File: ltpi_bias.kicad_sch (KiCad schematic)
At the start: 18 parts

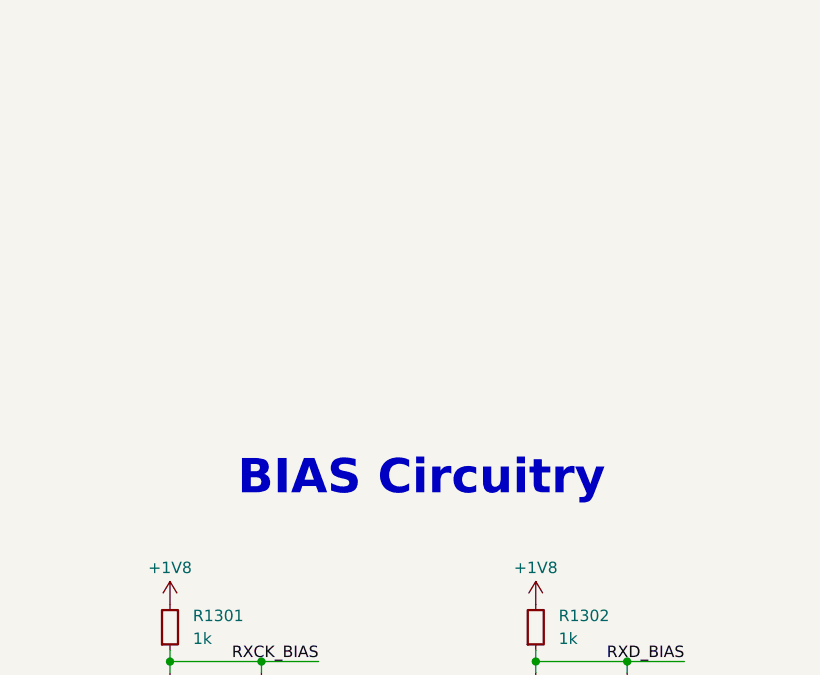
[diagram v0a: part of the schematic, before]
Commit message: [#100282] Add missing schematic sheet names and align them all
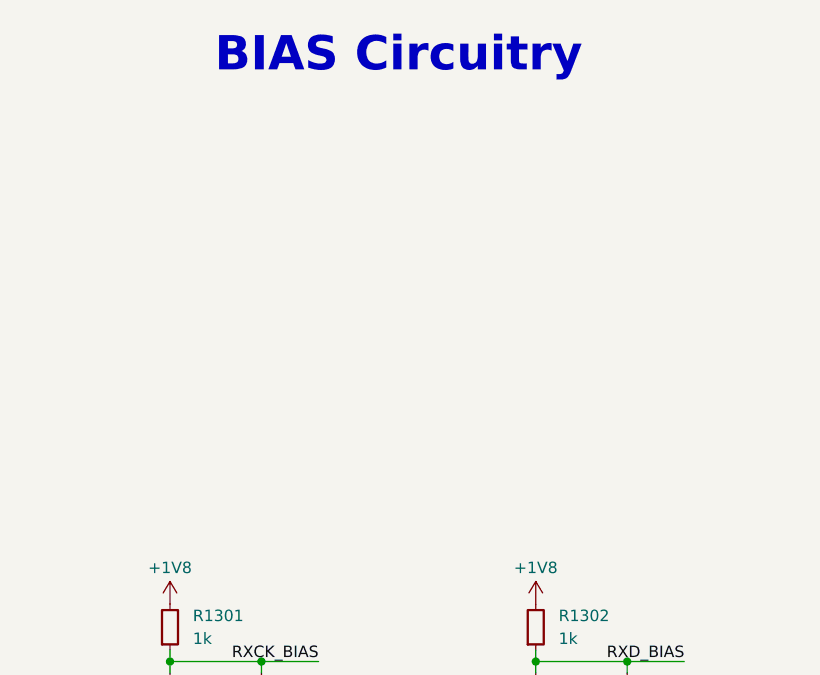
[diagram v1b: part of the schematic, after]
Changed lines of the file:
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@@
 	(text "BIAS Circuitry"
 		(exclude_from_sim no)
-		(at 213.36 85.09 0)
+		(at 210.82 38.1 0)
 		(effects
 			(font

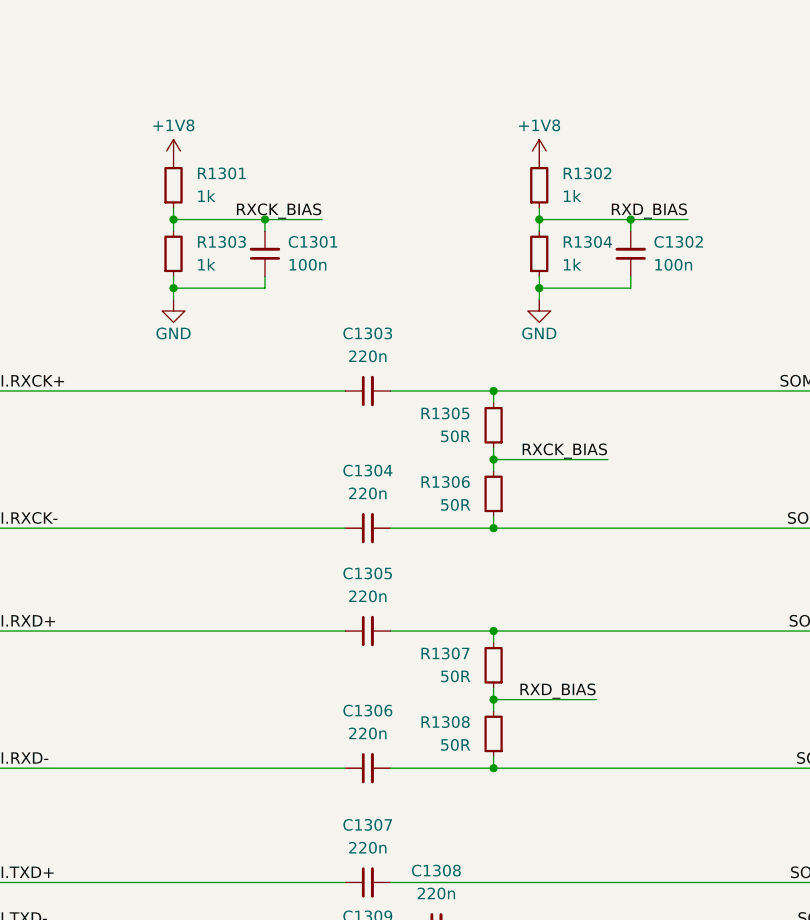
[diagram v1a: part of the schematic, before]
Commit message: [#100501] Replace 50R resistors with 49R9 in LTPI bias circuit
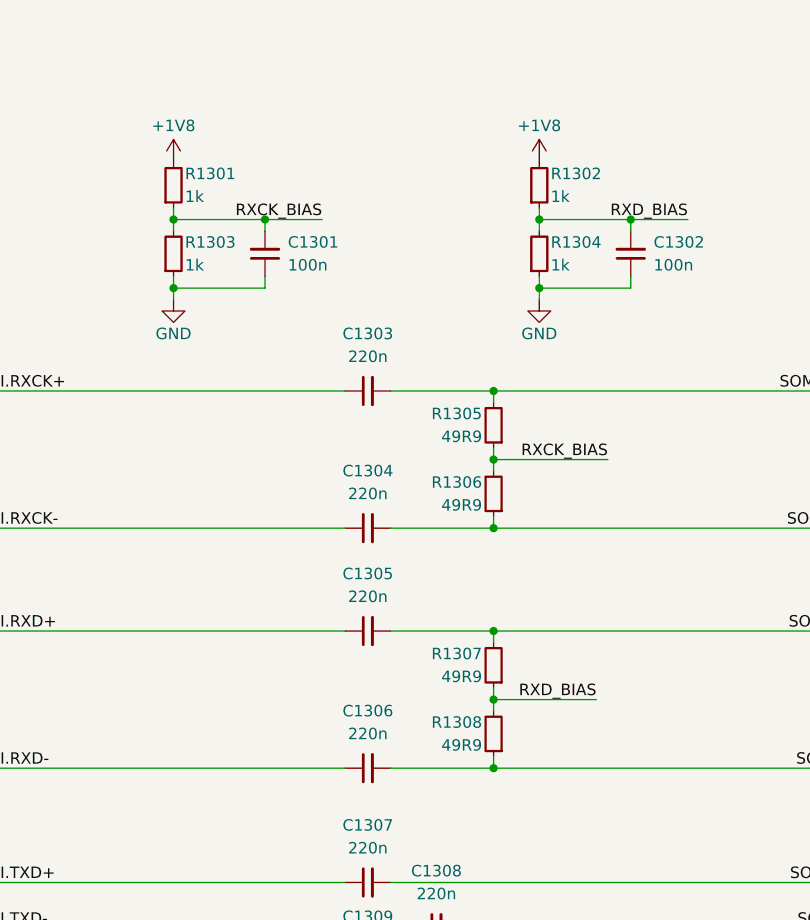
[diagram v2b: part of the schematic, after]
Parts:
- removed R1305, R1306, R1307, R1308: R_50R_0402, antmicro-footprints:R_0402_1005Metric, symbol antmicroResistors0402:R_50R_0402
- added R1305, R1306, R1307, R1308: R_49R9_0402, antmicro-footprints:R_0402_1005Metric, symbol antmicroResistors0402:R_49R9_0402
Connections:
- net RXCK_BIAS: now also R1305.1, R1306.2
- net RXD_BIAS: now also R1307.1, R1308.2
- net SOM_LTPI.RXCK+: now also R1305.2
- net SOM_LTPI.RXCK-: now also R1306.1
- net SOM_LTPI.RXD+: now also R1307.2
- net SOM_LTPI.RXD-: now also R1308.1

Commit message: [#100501] Reannotate schematic
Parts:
- renumbered C1310 to C100, C1301 to C91, C1302 to C92, C1303 to C93, C1304 to C94, C1305 to C95, C1306 to C96, C1307 to C97, C1308 to C98, C1309 to C99, R1301 to R137, R1302 to R138, R1303 to R139, R1304 to R140, R1305 to R141, R1306 to R142, R1307 to R143, R1308 to R144
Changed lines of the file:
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@@
 		(in_pos_files yes)
 		(dnp no)
-		(property "Reference" "#PWR01301"
+		(property "Reference" "#PWR0156"
 			(at 200.66 101.6 0)
 			(hide yes)
@@
 			(project "altera-modular-agilex-5-dc-scm"
 				(path "/6bb9d978-a328-4b30-874b-55170a976185/65eda2d2-086a-48f2-af4e-47077a805913"
-					(reference "#PWR01301")
+					(reference "#PWR0156")
 					(unit 1)
 				)
@@
 		(in_pos_files yes)
 		(dnp no)
-		(property "Reference" "R1306"
+		(property "Reference" "R142"
 			(at 219.71 134.62 90)
 			(show_name no)
@@
 			(project "altera-modular-agilex-5-dc-scm"
 				(path "/6bb9d978-a328-4b30-874b-55170a976185/65eda2d2-086a-48f2-af4e-47077a805913"
-					(reference "R1306")
+					(reference "R142")
 					(unit 1)
 				)
@@
 		(dnp no)
 		(fields_autoplaced yes)
-		(property "Reference" "C1304"
+		(property "Reference" "C94"
 			(at 207.0163 133.35 0)
 			(show_name no)
@@
 			(project "altera-modular-agilex-5-dc-scm"
 				(path "/6bb9d978-a328-4b30-874b-55170a976185/65eda2d2-086a-48f2-af4e-47077a805913"
-					(reference "C1304")
+					(reference "C94")
 					(unit 1)
 				)
@@
 		(dnp no)
 		(fields_autoplaced yes)
-		(property "Reference" "C1303"
+		(property "Reference" "C93"
 			(at 207.0163 118.11 0)
 			(show_name no)
@@
 			(project "altera-modular-agilex-5-dc-scm"
 				(path "/6bb9d978-a328-4b30-874b-55170a976185/65eda2d2-086a-48f2-af4e-47077a805913"
-					(reference "C1303")
+					(reference "C93")
 					(unit 1)
 				)
@@
 		(dnp no)
 		(fields_autoplaced yes)
-		(property "Reference" "C1306"
+		(property "Reference" "C96"
 			(at 207.0163 160.02 0)
 			(show_name no)
@@
 			(project "altera-modular-agilex-5-dc-scm"
 				(path "/6bb9d978-a328-4b30-874b-55170a976185/65eda2d2-086a-48f2-af4e-47077a805913"
-					(reference "C1306")
+					(reference "C96")
 					(unit 1)
 				)
@@
 		(dnp no)
 		(fields_autoplaced yes)
-		(property "Reference" "C1305"
+		(property "Reference" "C95"
 			(at 207.0163 144.78 0)
 			(show_name no)
@@
 			(project "altera-modular-agilex-5-dc-scm"
 				(path "/6bb9d978-a328-4b30-874b-55170a976185/65eda2d2-086a-48f2-af4e-47077a805913"
-					(reference "C1305")
+					(reference "C95")
 					(unit 1)
 				)
@@
 		(in_pos_files yes)
 		(dnp no)
-		(property "Reference" "#PWR01304"
+		(property "Reference" "#PWR0159"
 			(at 234.95 116.84 0)
 			(hide yes)
@@
 			(project "altera-modular-agilex-5-dc-scm"
 				(path "/6bb9d978-a328-4b30-874b-55170a976185/65eda2d2-086a-48f2-af4e-47077a805913"
-					(reference "#PWR01304")
+					(reference "#PWR0159")
 					(unit 1)
 				)
@@
 		(dnp no)
 		(fields_autoplaced yes)
-		(property "Reference" "C1309"
+		(property "Reference" "C99"
 			(at 207.0163 182.88 0)
 			(show_name no)
@@
 			(project "altera-modular-agilex-5-dc-scm"
 				(path "/6bb9d978-a328-4b30-874b-55170a976185/65eda2d2-086a-48f2-af4e-47077a805913"
-					(reference "C1309")
+					(reference "C99")
 					(unit 1)
 				)
@@
 		(in_pos_files yes)
 		(dnp no)
-		(property "Reference" "R1305"
+		(property "Reference" "R141"
 			(at 219.71 127 90)
 			(show_name no)
@@
 			(project "altera-modular-agilex-5-dc-scm"
 				(path "/6bb9d978-a328-4b30-874b-55170a976185/65eda2d2-086a-48f2-af4e-47077a805913"
-					(reference "R1305")
+					(reference "R141")
 					(unit 1)
 				)
@@
 		(dnp no)
 		(fields_autoplaced yes)
-		(property "Reference" "C1307"
+		(property "Reference" "C97"
 			(at 207.0163 172.72 0)
 			(show_name no)
@@
 			(project "altera-modular-agilex-5-dc-scm"
 				(path "/6bb9d978-a328-4b30-874b-55170a976185/65eda2d2-086a-48f2-af4e-47077a805913"
-					(reference "C1307")
+					(reference "C97")
 					(unit 1)
 				)
@@
 		(in_pos_files yes)
 		(dnp no)
-		(property "Reference" "R1303"
+		(property "Reference" "R139"
 			(at 186.69 107.95 90)
 			(show_name no)
@@
 			(project "altera-modular-agilex-5-dc-scm"
 				(path "/6bb9d978-a328-4b30-874b-55170a976185/65eda2d2-086a-48f2-af4e-47077a805913"
-					(reference "R1303")
+					(reference "R139")
 					(unit 1)
 				)
@@
 		(in_pos_files yes)
 		(dnp no)
-		(property "Reference" "#PWR01302"
+		(property "Reference" "#PWR0157"
 			(at 241.3 101.6 0)
 			(hide yes)
@@
 			(project "altera-modular-agilex-5-dc-scm"
 				(path "/6bb9d978-a328-4b30-874b-55170a976185/65eda2d2-086a-48f2-af4e-47077a805913"
-					(reference "#PWR01302")
+					(reference "#PWR0157")
 					(unit 1)
 				)
@@
 		(in_pos_files yes)
 		(dnp no)
-		(property "Reference" "R1301"
+		(property "Reference" "R137"
 			(at 186.69 100.33 90)
 			(show_name no)
@@
 			(project "altera-modular-agilex-5-dc-scm"
 				(path "/6bb9d978-a328-4b30-874b-55170a976185/65eda2d2-086a-48f2-af4e-47077a805913"
-					(reference "R1301")
+					(reference "R137")
 					(unit 1)
 				)
@@
 		(dnp no)
 		(fields_autoplaced yes)
-		(property "Reference" "C1310"
+		(property "Reference" "C100"
 			(at 214.6363 187.96 0)
 			(show_name no)
@@
 			(project "altera-modular-agilex-5-dc-scm"
 				(path "/6bb9d978-a328-4b30-874b-55170a976185/65eda2d2-086a-48f2-af4e-47077a805913"
-					(reference "C1310")
+					(reference "C100")
 					(unit 1)
 				)
@@
 		(dnp no)
 		(fields_autoplaced yes)
-		(property "Reference" "C1308"
+		(property "Reference" "C98"
 			(at 214.6363 177.8 0)
 			(show_name no)
@@
 			(project "altera-modular-agilex-5-dc-scm"
 				(path "/6bb9d978-a328-4b30-874b-55170a976185/65eda2d2-086a-48f2-af4e-47077a805913"
-					(reference "C1308")
+					(reference "C98")
 					(unit 1)
 				)
@@
 		(in_pos_files yes)
 		(dnp no)
-		(property "Reference" "R1302"
+		(property "Reference" "R138"
 			(at 227.33 100.33 90)
 			(show_name no)
@@
 			(project "altera-modular-agilex-5-dc-scm"
 				(path "/6bb9d978-a328-4b30-874b-55170a976185/65eda2d2-086a-48f2-af4e-47077a805913"
-					(reference "R1302")
+					(reference "R138")
 					(unit 1)
 				)
@@
 		(dnp no)
 		(fields_autoplaced yes)
-		(property "Reference" "C1301"
+		(property "Reference" "C91"
 			(at 198.12 107.9436 90)
 			(show_name no)
@@
 			(project "altera-modular-agilex-5-dc-scm"
 				(path "/6bb9d978-a328-4b30-874b-55170a976185/65eda2d2-086a-48f2-af4e-47077a805913"
-					(reference "C1301")
+					(reference "C91")
 					(unit 1)
 				)
@@
 		(dnp no)
 		(fields_autoplaced yes)
-		(property "Reference" "C1302"
+		(property "Reference" "C92"
 			(at 238.76 107.9436 90)
 			(show_name no)
@@
 			(project "altera-modular-agilex-5-dc-scm"
 				(path "/6bb9d978-a328-4b30-874b-55170a976185/65eda2d2-086a-48f2-af4e-47077a805913"
-					(reference "C1302")
+					(reference "C92")
 					(unit 1)
 				)
@@
 		(in_pos_files yes)
 		(dnp no)
-		(property "Reference" "#PWR01303"
+		(property "Reference" "#PWR0158"
 			(at 194.31 116.84 0)
 			(hide yes)
@@
 			(project "altera-modular-agilex-5-dc-scm"
 				(path "/6bb9d978-a328-4b30-874b-55170a976185/65eda2d2-086a-48f2-af4e-47077a805913"
-					(reference "#PWR01303")
+					(reference "#PWR0158")
 					(unit 1)
 				)
@@
 		(in_pos_files yes)
 		(dnp no)
-		(property "Reference" "R1307"
+		(property "Reference" "R143"
 			(at 219.71 153.67 90)
 			(show_name no)
@@
 			(project "altera-modular-agilex-5-dc-scm"
 				(path "/6bb9d978-a328-4b30-874b-55170a976185/65eda2d2-086a-48f2-af4e-47077a805913"
-					(reference "R1307")
+					(reference "R143")
 					(unit 1)
 				)
@@
 		(in_pos_files yes)
 		(dnp no)
-		(property "Reference" "R1308"
+		(property "Reference" "R144"
 			(at 219.71 161.29 90)
 			(show_name no)
@@
 			(project "altera-modular-agilex-5-dc-scm"
 				(path "/6bb9d978-a328-4b30-874b-55170a976185/65eda2d2-086a-48f2-af4e-47077a805913"
-					(reference "R1308")
+					(reference "R144")
 					(unit 1)
 				)
@@
 		(in_pos_files yes)
 		(dnp no)
-		(property "Reference" "R1304"
+		(property "Reference" "R140"
 			(at 227.33 107.95 90)
 			(show_name no)
@@
 			(project "altera-modular-agilex-5-dc-scm"
 				(path "/6bb9d978-a328-4b30-874b-55170a976185/65eda2d2-086a-48f2-af4e-47077a805913"
-					(reference "R1304")
+					(reference "R140")
 					(unit 1)
 				)

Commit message: [#100501] Reannotate schematic
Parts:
- renumbered C96 to C100, C97 to C101, C98 to C102, C99 to C103, C100 to C104, C91 to C95, C92 to C96, C93 to C97, C94 to C98, C95 to C99, R137 to R171, R138 to R172, R139 to R173, R140 to R174, R141 to R175, R142 to R176, R143 to R177, R144 to R178
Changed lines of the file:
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@@
 		(in_pos_files yes)
 		(dnp no)
-		(property "Reference" "#PWR0156"
+		(property "Reference" "#PWR0155"
 			(at 200.66 101.6 0)
 			(hide yes)
@@
 			(project "altera-modular-agilex-5-dc-scm"
 				(path "/6bb9d978-a328-4b30-874b-55170a976185/65eda2d2-086a-48f2-af4e-47077a805913"
-					(reference "#PWR0156")
+					(reference "#PWR0155")
 					(unit 1)
 				)
@@
 		(in_pos_files yes)
 		(dnp no)
-		(property "Reference" "R142"
+		(property "Reference" "R176"
 			(at 219.71 134.62 90)
 			(show_name no)
@@
 			(project "altera-modular-agilex-5-dc-scm"
 				(path "/6bb9d978-a328-4b30-874b-55170a976185/65eda2d2-086a-48f2-af4e-47077a805913"
-					(reference "R142")
+					(reference "R176")
 					(unit 1)
 				)
@@
 		(dnp no)
 		(fields_autoplaced yes)
-		(property "Reference" "C94"
+		(property "Reference" "C98"
 			(at 207.0163 133.35 0)
 			(show_name no)
@@
 			(project "altera-modular-agilex-5-dc-scm"
 				(path "/6bb9d978-a328-4b30-874b-55170a976185/65eda2d2-086a-48f2-af4e-47077a805913"
-					(reference "C94")
+					(reference "C98")
 					(unit 1)
 				)
@@
 		(dnp no)
 		(fields_autoplaced yes)
-		(property "Reference" "C93"
+		(property "Reference" "C97"
 			(at 207.0163 118.11 0)
 			(show_name no)
@@
 			(project "altera-modular-agilex-5-dc-scm"
 				(path "/6bb9d978-a328-4b30-874b-55170a976185/65eda2d2-086a-48f2-af4e-47077a805913"
-					(reference "C93")
+					(reference "C97")
 					(unit 1)
 				)
@@
 		(dnp no)
 		(fields_autoplaced yes)
-		(property "Reference" "C96"
+		(property "Reference" "C100"
 			(at 207.0163 160.02 0)
 			(show_name no)
@@
 			(project "altera-modular-agilex-5-dc-scm"
 				(path "/6bb9d978-a328-4b30-874b-55170a976185/65eda2d2-086a-48f2-af4e-47077a805913"
-					(reference "C96")
+					(reference "C100")
 					(unit 1)
 				)
@@
 		(dnp no)
 		(fields_autoplaced yes)
-		(property "Reference" "C95"
+		(property "Reference" "C99"
 			(at 207.0163 144.78 0)
 			(show_name no)
@@
 			(project "altera-modular-agilex-5-dc-scm"
 				(path "/6bb9d978-a328-4b30-874b-55170a976185/65eda2d2-086a-48f2-af4e-47077a805913"
-					(reference "C95")
+					(reference "C99")
 					(unit 1)
 				)
@@
 		(in_pos_files yes)
 		(dnp no)
-		(property "Reference" "#PWR0159"
+		(property "Reference" "#PWR0158"
 			(at 234.95 116.84 0)
 			(hide yes)
@@
 			(project "altera-modular-agilex-5-dc-scm"
 				(path "/6bb9d978-a328-4b30-874b-55170a976185/65eda2d2-086a-48f2-af4e-47077a805913"
-					(reference "#PWR0159")
+					(reference "#PWR0158")
 					(unit 1)
 				)
@@
 		(dnp no)
 		(fields_autoplaced yes)
-		(property "Reference" "C99"
+		(property "Reference" "C103"
 			(at 207.0163 182.88 0)
 			(show_name no)
@@
 			(project "altera-modular-agilex-5-dc-scm"
 				(path "/6bb9d978-a328-4b30-874b-55170a976185/65eda2d2-086a-48f2-af4e-47077a805913"
-					(reference "C99")
+					(reference "C103")
 					(unit 1)
 				)
@@
 		(in_pos_files yes)
 		(dnp no)
-		(property "Reference" "R141"
+		(property "Reference" "R175"
 			(at 219.71 127 90)
 			(show_name no)
@@
 			(project "altera-modular-agilex-5-dc-scm"
 				(path "/6bb9d978-a328-4b30-874b-55170a976185/65eda2d2-086a-48f2-af4e-47077a805913"
-					(reference "R141")
+					(reference "R175")
 					(unit 1)
 				)
@@
 		(dnp no)
 		(fields_autoplaced yes)
-		(property "Reference" "C97"
+		(property "Reference" "C101"
 			(at 207.0163 172.72 0)
 			(show_name no)
@@
 			(project "altera-modular-agilex-5-dc-scm"
 				(path "/6bb9d978-a328-4b30-874b-55170a976185/65eda2d2-086a-48f2-af4e-47077a805913"
-					(reference "C97")
+					(reference "C101")
 					(unit 1)
 				)
@@
 		(in_pos_files yes)
 		(dnp no)
-		(property "Reference" "R139"
+		(property "Reference" "R173"
 			(at 186.69 107.95 90)
 			(show_name no)
@@
 			(project "altera-modular-agilex-5-dc-scm"
 				(path "/6bb9d978-a328-4b30-874b-55170a976185/65eda2d2-086a-48f2-af4e-47077a805913"
-					(reference "R139")
+					(reference "R173")
 					(unit 1)
 				)
@@
 		(in_pos_files yes)
 		(dnp no)
-		(property "Reference" "#PWR0157"
+		(property "Reference" "#PWR0156"
 			(at 241.3 101.6 0)
 			(hide yes)
@@
 			(project "altera-modular-agilex-5-dc-scm"
 				(path "/6bb9d978-a328-4b30-874b-55170a976185/65eda2d2-086a-48f2-af4e-47077a805913"
-					(reference "#PWR0157")
+					(reference "#PWR0156")
 					(unit 1)
 				)
@@
 		(in_pos_files yes)
 		(dnp no)
-		(property "Reference" "R137"
+		(property "Reference" "R171"
 			(at 186.69 100.33 90)
 			(show_name no)
@@
 			(project "altera-modular-agilex-5-dc-scm"
 				(path "/6bb9d978-a328-4b30-874b-55170a976185/65eda2d2-086a-48f2-af4e-47077a805913"
-					(reference "R137")
+					(reference "R171")
 					(unit 1)
 				)
@@
 		(dnp no)
 		(fields_autoplaced yes)
-		(property "Reference" "C100"
+		(property "Reference" "C104"
 			(at 214.6363 187.96 0)
 			(show_name no)
@@
 			(project "altera-modular-agilex-5-dc-scm"
 				(path "/6bb9d978-a328-4b30-874b-55170a976185/65eda2d2-086a-48f2-af4e-47077a805913"
-					(reference "C100")
+					(reference "C104")
 					(unit 1)
 				)
@@
 		(dnp no)
 		(fields_autoplaced yes)
-		(property "Reference" "C98"
+		(property "Reference" "C102"
 			(at 214.6363 177.8 0)
 			(show_name no)
@@
 			(project "altera-modular-agilex-5-dc-scm"
 				(path "/6bb9d978-a328-4b30-874b-55170a976185/65eda2d2-086a-48f2-af4e-47077a805913"
-					(reference "C98")
+					(reference "C102")
 					(unit 1)
 				)
@@
 		(in_pos_files yes)
 		(dnp no)
-		(property "Reference" "R138"
+		(property "Reference" "R172"
 			(at 227.33 100.33 90)
 			(show_name no)
@@
 			(project "altera-modular-agilex-5-dc-scm"
 				(path "/6bb9d978-a328-4b30-874b-55170a976185/65eda2d2-086a-48f2-af4e-47077a805913"
-					(reference "R138")
+					(reference "R172")
 					(unit 1)
 				)
@@
 		(dnp no)
 		(fields_autoplaced yes)
-		(property "Reference" "C91"
+		(property "Reference" "C95"
 			(at 198.12 107.9436 90)
 			(show_name no)
@@
 			(project "altera-modular-agilex-5-dc-scm"
 				(path "/6bb9d978-a328-4b30-874b-55170a976185/65eda2d2-086a-48f2-af4e-47077a805913"
-					(reference "C91")
+					(reference "C95")
 					(unit 1)
 				)
@@
 		(dnp no)
 		(fields_autoplaced yes)
-		(property "Reference" "C92"
+		(property "Reference" "C96"
 			(at 238.76 107.9436 90)
 			(show_name no)
@@
 			(project "altera-modular-agilex-5-dc-scm"
 				(path "/6bb9d978-a328-4b30-874b-55170a976185/65eda2d2-086a-48f2-af4e-47077a805913"
-					(reference "C92")
+					(reference "C96")
 					(unit 1)
 				)
@@
 		(in_pos_files yes)
 		(dnp no)
-		(property "Reference" "#PWR0158"
+		(property "Reference" "#PWR0157"
 			(at 194.31 116.84 0)
 			(hide yes)
@@
 			(project "altera-modular-agilex-5-dc-scm"
 				(path "/6bb9d978-a328-4b30-874b-55170a976185/65eda2d2-086a-48f2-af4e-47077a805913"
-					(reference "#PWR0158")
+					(reference "#PWR0157")
 					(unit 1)
 				)
@@
 		(in_pos_files yes)
 		(dnp no)
-		(property "Reference" "R143"
+		(property "Reference" "R177"
 			(at 219.71 153.67 90)
 			(show_name no)
@@
 			(project "altera-modular-agilex-5-dc-scm"
 				(path "/6bb9d978-a328-4b30-874b-55170a976185/65eda2d2-086a-48f2-af4e-47077a805913"
-					(reference "R143")
+					(reference "R177")
 					(unit 1)
 				)
@@
 		(in_pos_files yes)
 		(dnp no)
-		(property "Reference" "R144"
+		(property "Reference" "R178"
 			(at 219.71 161.29 90)
 			(show_name no)
@@
 			(project "altera-modular-agilex-5-dc-scm"
 				(path "/6bb9d978-a328-4b30-874b-55170a976185/65eda2d2-086a-48f2-af4e-47077a805913"
-					(reference "R144")
+					(reference "R178")
 					(unit 1)
 				)
@@
 		(in_pos_files yes)
 		(dnp no)
-		(property "Reference" "R140"
+		(property "Reference" "R174"
 			(at 227.33 107.95 90)
 			(show_name no)
@@
 			(project "altera-modular-agilex-5-dc-scm"
 				(path "/6bb9d978-a328-4b30-874b-55170a976185/65eda2d2-086a-48f2-af4e-47077a805913"
-					(reference "R140")
+					(reference "R174")
 					(unit 1)
 				)
